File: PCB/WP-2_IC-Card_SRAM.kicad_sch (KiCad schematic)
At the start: 20 parts, among them J1 SMS-138-01-G-S, SW1 CUS-14TB, U1 AS6C4008

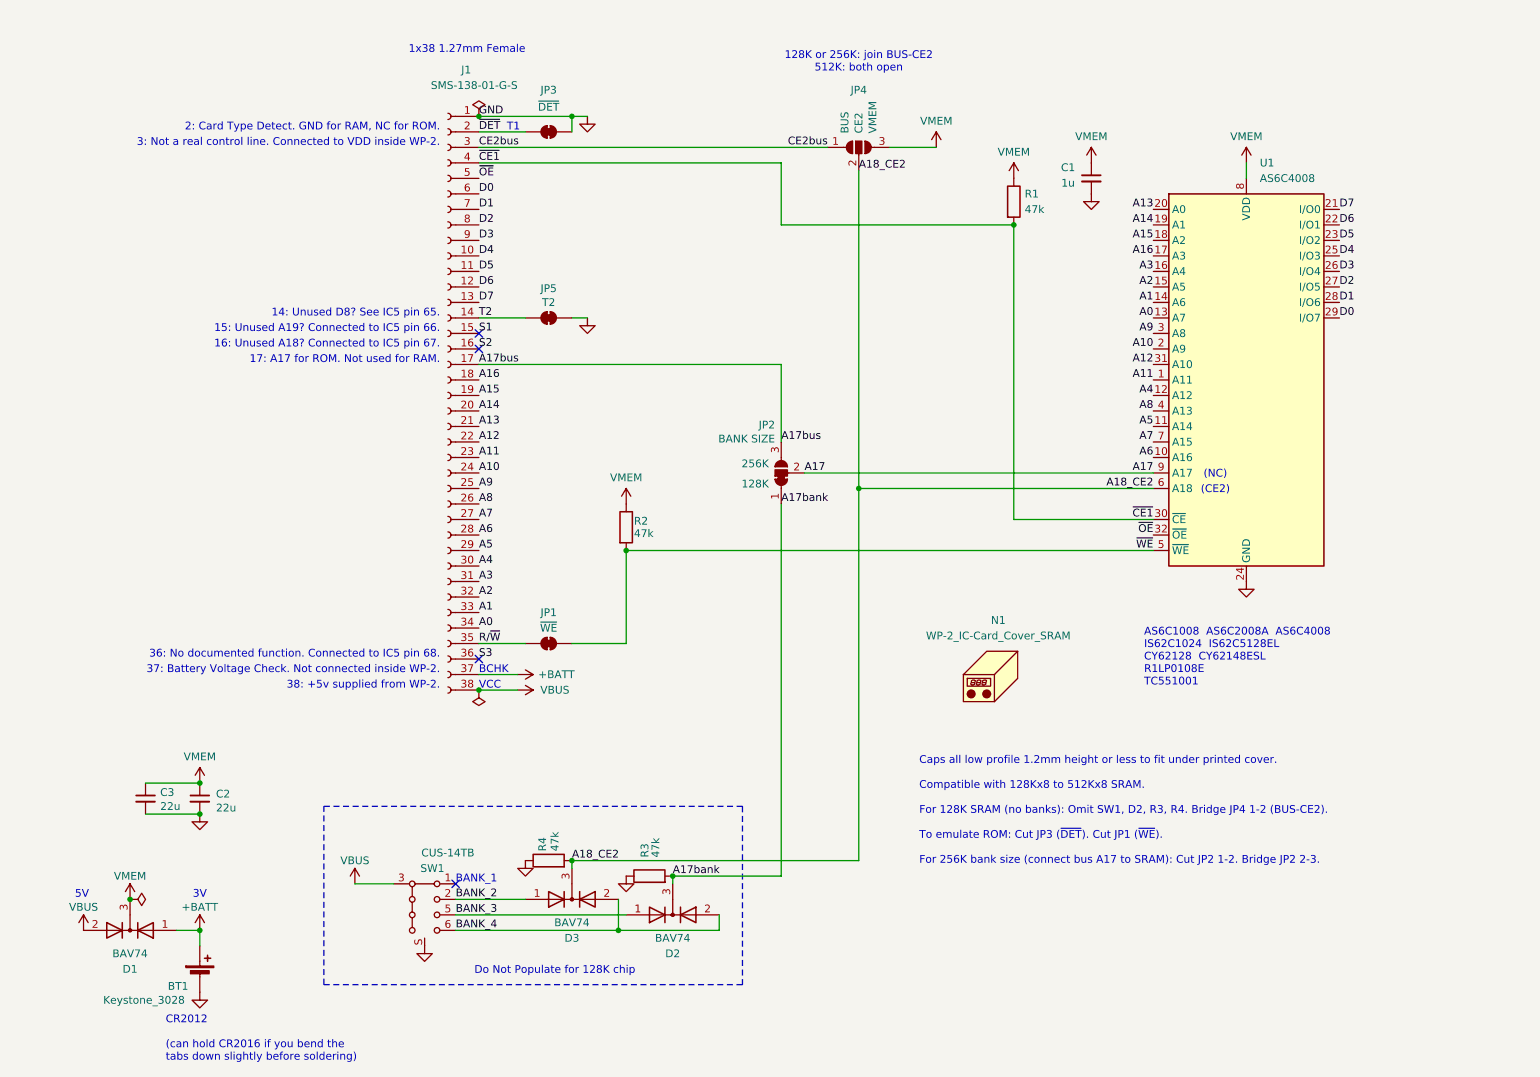
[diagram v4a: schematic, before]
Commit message: sram: resistors 100k, silkscreen, pics
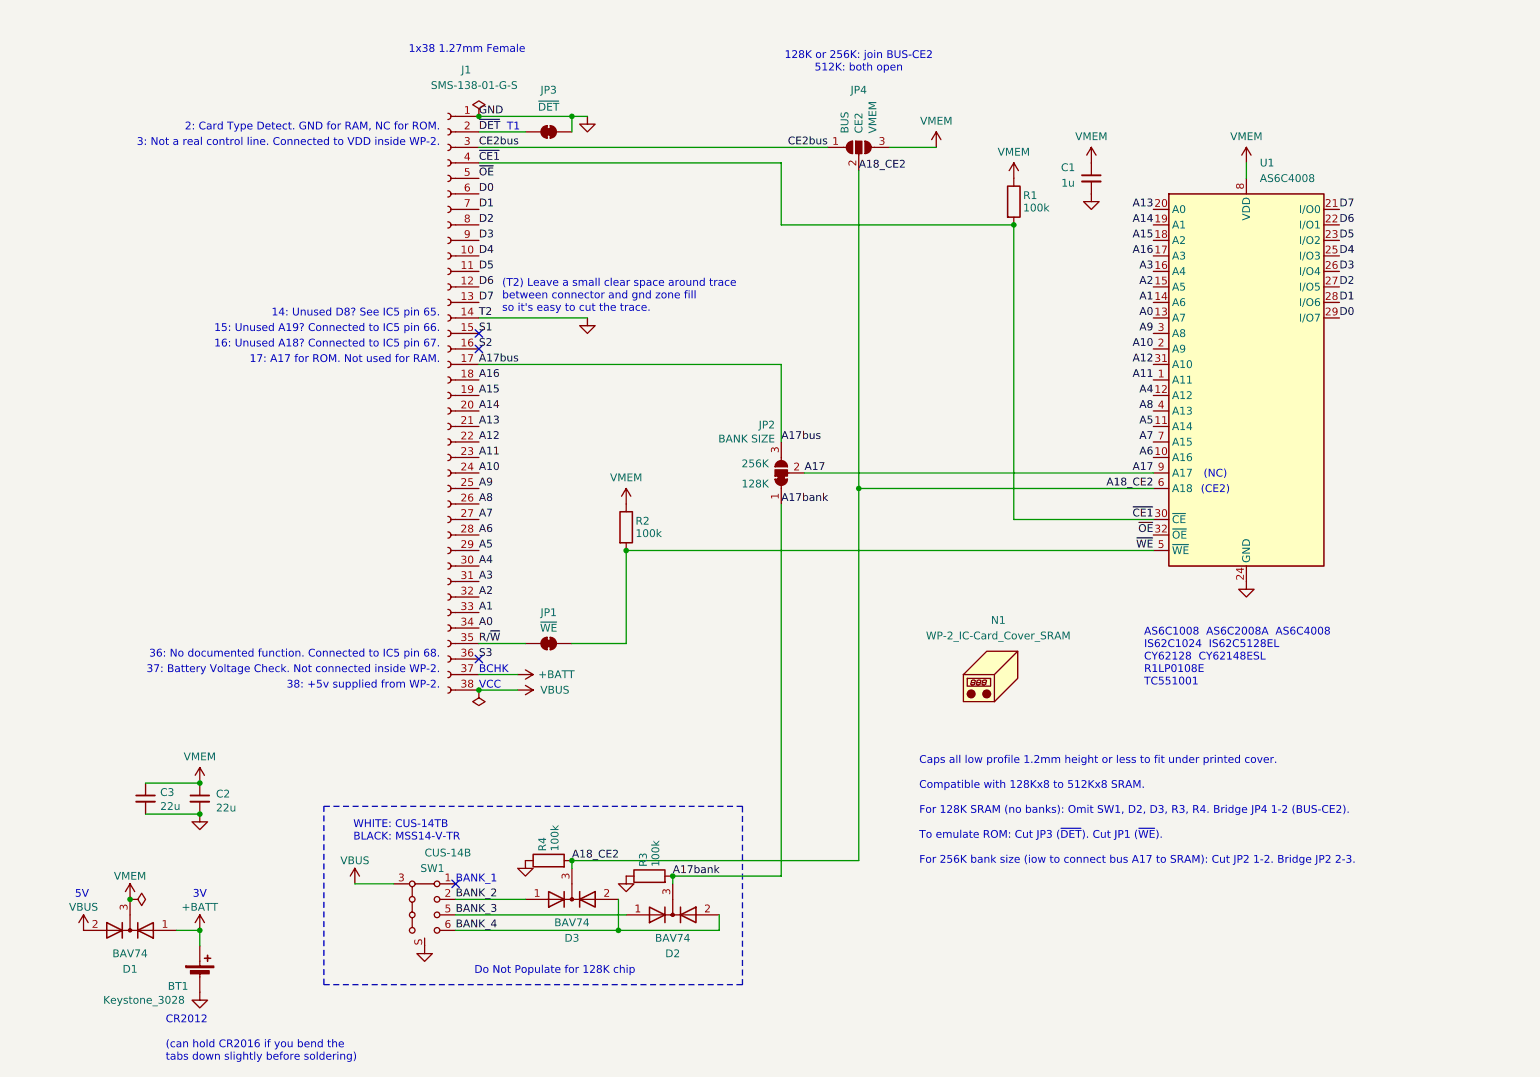
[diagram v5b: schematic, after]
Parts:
- removed JP5: T2, 000_LOCAL:SolderJumper-2_Bridged, symbol 000_LOCAL:SolderJumper_2_Bridged
- R1, R2, R3, R4: value 47k -> 100k; MPN RMCF0805FT47K0 -> RC0805FR-07100KL
- SW1: value CUS-14TB -> CUS-14B
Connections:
- net T2 is gone; now on net GND: J1.14 (Pin_14)
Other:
- note added: "(T2) Leave a small clear space around trace between connector and gnd zone fill so it's easy to cut the trace."
- note added: "Caps all low profile 1.2mm height or less to fit under printed cover. Compatible with 128Kx8 to 512Kx8 SRAM. For 128K SRAM (no banks): Omit SW1, D2, D3, R3, R4. Bridge JP4 1-2 (BUS-CE2). To emulate ROM: Cut JP3 (~{DET}). Cut JP1 (~{WE}). For 256K bank size (iow to connect bus A17 to SRAM): Cut JP2 1-2. Bridge JP2 2-3."
- note added: "WHITE: CUS-14TB BLACK: MSS14-V-TR"
- note removed: "Caps all low profile 1.2mm height or less to fit under printed cover. Compatible with 128Kx8 to 512Kx8 SRAM. For 128K SRAM (no banks): Omit SW1, D2, R3, R4. Bridge JP4 1-2 (BUS-CE2). To emulate ROM: Cut JP3 (~{DET}). Cut JP1 (~{WE}). For 256K bank size (connect bus A17 to SRAM): Cut JP2 1-2. Bridge JP2 2-3."

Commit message: silkscreens, board outlines, switch slider, covers fitment, copper to edge
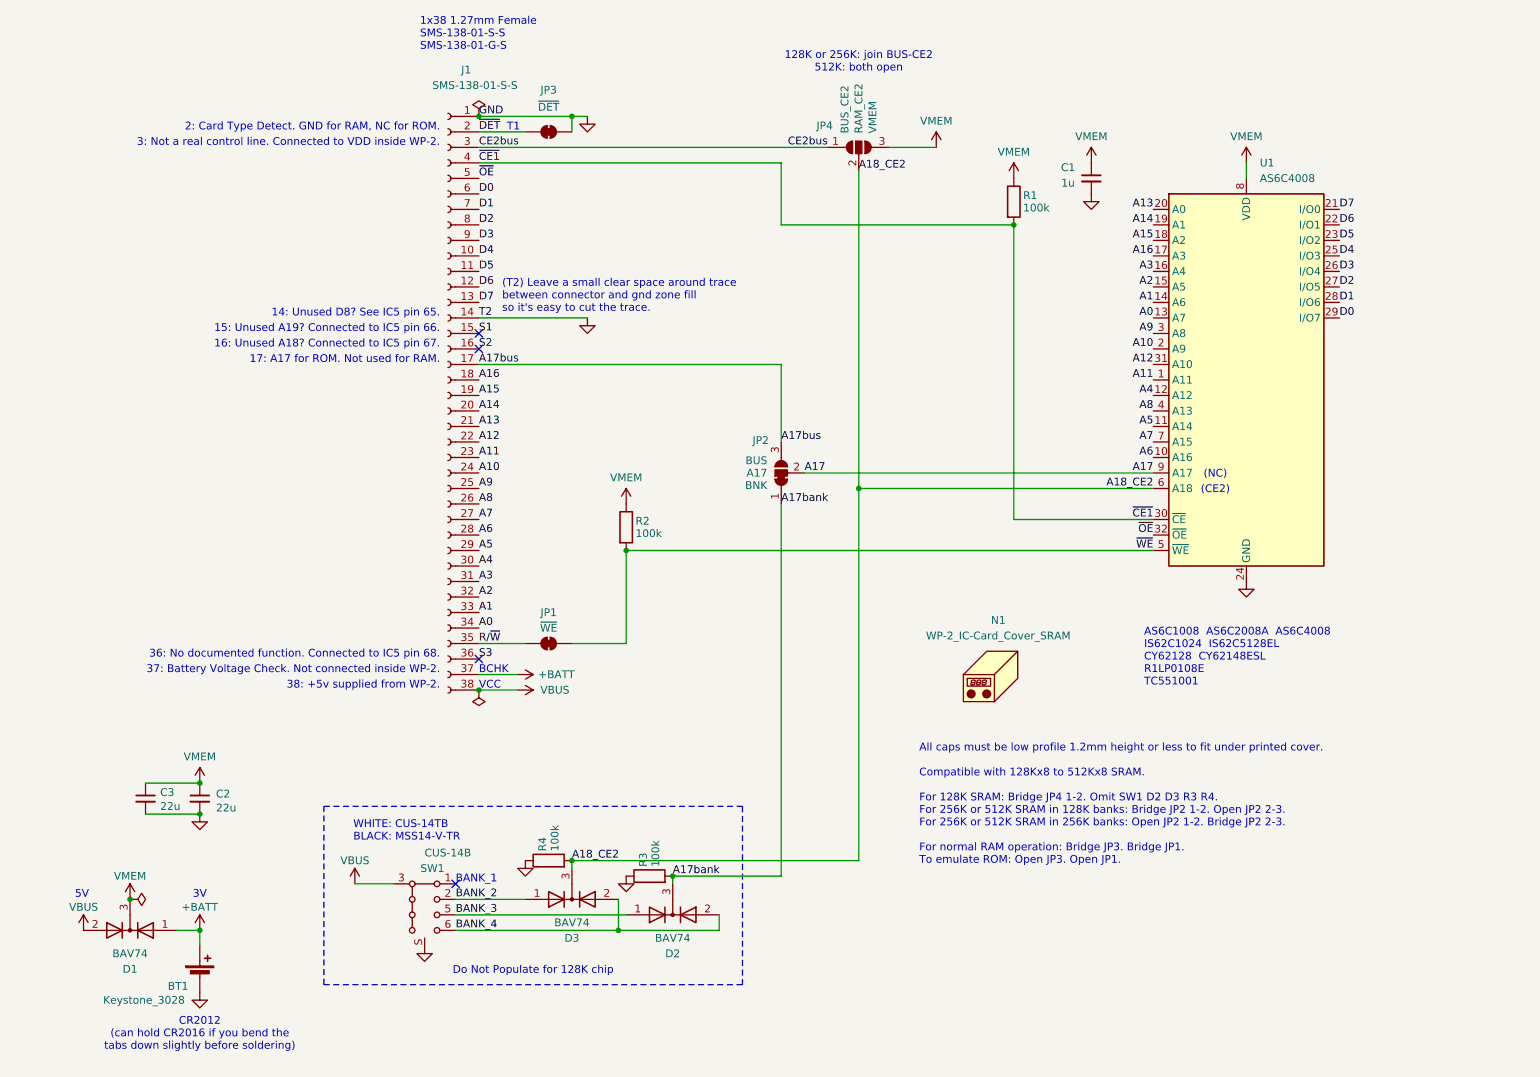
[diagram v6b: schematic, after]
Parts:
- J1: value SMS-138-01-G-S -> SMS-138-01-S-S; footprint 000_LOCAL:SMS-138-01-x-x_pcb_edge -> 000_LOCAL:SMS-138-01-x-S_pcb_edge
- JP2: value BANK SIZE -> A17; Label_1-2 128K -> BNK; Label_2-3 256K -> BUS
- JP4: value CE2 -> RAM_CE2; Label_1-2 BUS -> BUS_CE2
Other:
- note added: "1x38 1.27mm Female SMS-138-01-S-S SMS-138-01-G-S"
- note added: "All caps must be low profile 1.2mm height or less to fit under printed cover. Compatible with 128Kx8 to 512Kx8 SRAM. For 128K SRAM: Bridge JP4 1-2. Omit SW1 D2 D3 R3 R4. For 256K or 512K SRAM in 128K banks: Bridge JP2 1-2. Open JP2 2-3. For 256K or 512K SRAM in 256K banks: Open JP2 1-2. Bridge JP2 2-3. For normal RAM operation: Bridge JP3. Bridge JP1. To emulate ROM: Open JP3. Open JP1."
- note removed: "1x38 1.27mm Female"
- note removed: "Caps all low profile 1.2mm height or less to fit under printed cover. Compatible with 128Kx8 to 512Kx8 SRAM. For 128K SRAM (no banks): Omit SW1, D2, D3, R3, R4. Bridge JP4 1-2 (BUS-CE2). To emulate ROM: Cut JP3 (~{DET}). Cut JP1 (~{WE}). For 256K bank size (iow to connect bus A17 to SRAM): Cut JP2 1-2. Bridge JP2 2-3."
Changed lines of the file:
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@@
 		)
 	)
-	(text "1x38 1.27mm Female"
+	(text "1x38 1.27mm Female\nSMS-138-01-S-S\nSMS-138-01-G-S"
 		(exclude_from_sim no)
-		(at 97.79 35.56 0)
+		(at 80.518 35.052 0)
 		(effects
 			(font
 				(size 1.27 1.27)
 			)
-			(justify right bottom)
+			(justify left bottom)
 		)
 	)
@@
 		)
 	)
-	(text "CR2012\n\n(can hold CR2016 if you bend the\ntabs down slightly before soldering)"
+	(text "CR2012\n(can hold CR2016 if you bend the\ntabs down slightly before soldering)"
 		(exclude_from_sim no)
-		(at 38.862 193.04 0)
+		(at 44.45 193.294 0)
 		(effects
 			(font
 				(size 1.27 1.27)
 			)
-			(justify left top)
+			(justify top)
 		)
 	)
@@
 		)
 	)
-	(text "Caps all low profile 1.2mm height or less to fit under printed cover.\n\nCompatible with 128Kx8 to 512Kx8 SRAM.\n\nFor 128K SRAM (no banks): Omit SW1, D2, D3, R3, R4. Bridge JP4 1-2 (BUS-CE2).\n\nTo emulate ROM: Cut JP3 (~{DET}). Cut JP1 (~{WE}).\n\nFor 256K bank size (iow to connect bus A17 to SRAM): Cut JP2 1-2. Bridge JP2 2-3."
+	(text "All caps must be low profile 1.2mm height or less to fit under printed cover.\n\nCompatible with 128Kx8 to 512Kx8 SRAM.\n\nFor 128K SRAM: Bridge JP4 1-2. Omit SW1 D2 D3 R3 R4.\nFor 256K or 512K SRAM in 128K banks: Bridge JP2 1-2. Open JP2 2-3.\nFor 256K or 512K SRAM in 256K banks: Open JP2 1-2. Bridge JP2 2-3.\n\nFor normal RAM operation: Bridge JP3. Bridge JP1.\nTo emulate ROM: Open JP3. Open JP1.\n"
 		(exclude_from_sim no)
 		(at 162.306 168.402 0)
@@
 	(text "Do Not Populate for 128K chip"
 		(exclude_from_sim no)
-		(at 102.616 186.436 0)
+		(at 99.06 186.436 0)
 		(effects
 			(font
@@
 			)
 		)
-		(property "Value" "SMS-138-01-G-S"
+		(property "Value" "SMS-138-01-S-S"
 			(at 96.52 40.64 0)
 			(effects
@@
 			)
 		)
-		(property "Footprint" "000_LOCAL:SMS-138-01-x-x_pcb_edge"
+		(property "Footprint" "000_LOCAL:SMS-138-01-x-S_pcb_edge"
 			(at 85.09 91.44 0)
 			(effects
@@
 		(dnp no)
 		(property "Reference" "JP2"
-			(at 138.684 96.266 90)
+			(at 137.668 98.806 90)
 			(effects
 				(font
@@
 			)
 		)
-		(property "Value" "BANK SIZE"
-			(at 138.684 98.552 90)
+		(property "Value" "A17"
+			(at 137.414 104.14 90)
 			(effects
 				(font
@@
 			)
 		)
-		(property "Label_1-2" "128K"
-			(at 137.668 105.918 90)
+		(property "Label_1-2" "BNK"
+			(at 137.414 106.172 90)
 			(effects
 				(font
@@
 			)
 		)
-		(property "Label_2-3" "256K"
-			(at 137.668 102.616 90)
+		(property "Label_2-3" "BUS"
+			(at 137.414 102.108 90)
 			(effects
 				(font
@@
 		(dnp no)
 		(property "Reference" "JP4"
-			(at 152.4 41.402 0)
+			(at 146.812 47.244 0)
 			(effects
 				(font
@@
 			)
 		)
-		(property "Value" "CE2"
+		(property "Value" "RAM_CE2"
 			(at 152.4 48.514 90)
 			(effects
@@
 			)
 		)
-		(property "Label_1-2" "BUS"
+		(property "Label_1-2" "BUS_CE2"
 			(at 150.114 48.514 90)
 			(effects

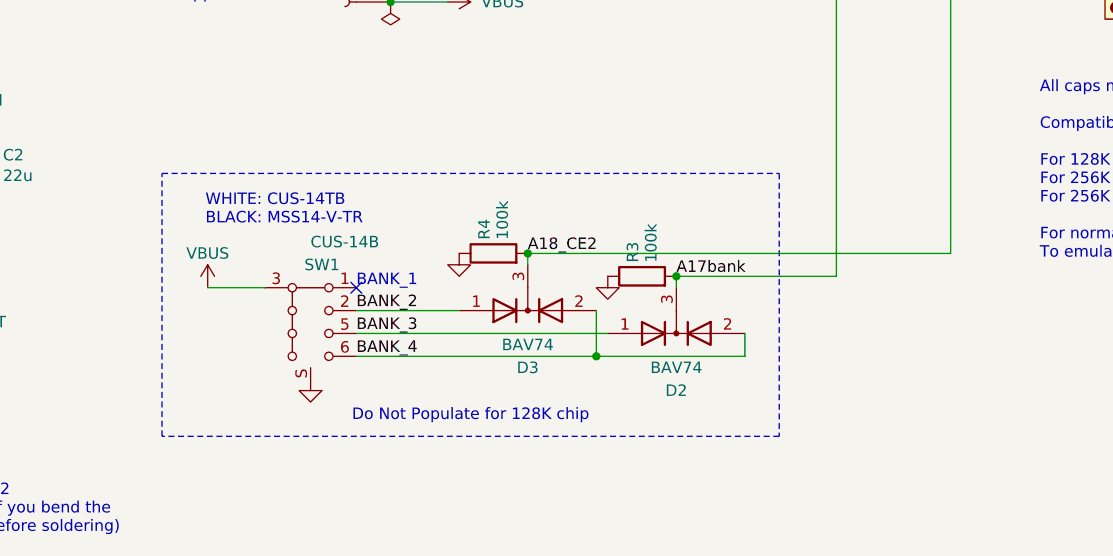
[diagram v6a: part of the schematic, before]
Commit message: MRAM: diodes, level shifters, ldo, docs
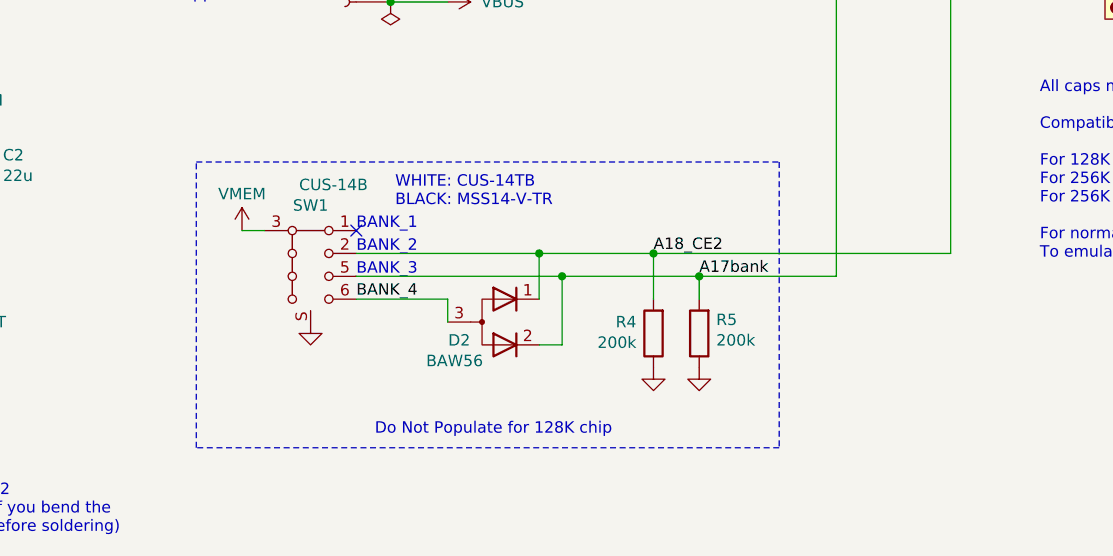
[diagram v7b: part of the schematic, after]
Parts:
- removed D2, D3: BAV74, 000_LOCAL:SOT-23, symbol 000_LOCAL:BAV170
- removed R3: 100k, 000_LOCAL:R_0805, symbol 000_LOCAL:R
- added D2: BAW56, 000_LOCAL:SOT-23, symbol 000_LOCAL:D_Dual_CommonAnode_KKA_Parallel
- added R5: 200k, 000_LOCAL:R_0805, symbol 000_LOCAL:R
- R4: value 100k -> 200k; MPN RC0805FR-07100KL -> RMCF0805FT200K
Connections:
- net BANK_2 is gone; now on net A18_CE2: SW1.2
- net BANK_3 is gone; now on net A17bank: SW1.5
- net A17bank: now also D2.2 (K), R5.2
- net A18_CE2: now also D2.1 (K)
- net BANK_4: now also D2.3 (A)
- net GND: now also R5.1
- net VBUS: no longer SW1.3 (C), SW1.4 (C)
- net VMEM: now also SW1.3 (C), SW1.4 (C)
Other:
- note added: "BANK_2"
- note added: "BANK_3"

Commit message: sram diodes
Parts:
- removed D2: BAW56, 000_LOCAL:SOT-23, symbol 000_LOCAL:D_Dual_CommonAnode_KKA_Parallel
- removed R5: 200k, 000_LOCAL:R_0805, symbol 000_LOCAL:R
- added D2, D3: BAV74, 000_LOCAL:SOT-23, symbol 000_LOCAL:BAV70
- added R3: 100k, 000_LOCAL:R_0805, symbol 000_LOCAL:R
- R4: value 200k -> 100k; MPN RMCF0805FT200K -> RC0805FR-07100KL
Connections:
- net A17bank: now also SW1.2, D2.3 (K), R3.2; no longer SW1.5
- net A18_CE2: now also SW1.5, D3.3 (K); no longer SW1.2
- net BANK_4: now also D2.2 (A), D3.1 (A)
- net GND: now also R3.1
- net R/~{W}: now also JP1.2 (B); no longer JP1.1 (A)
- net VBUS: now also SW1.3 (C), SW1.4 (C)
- net VMEM: no longer SW1.3 (C), SW1.4 (C)
- net ~{WE}: now also JP1.1 (A); no longer JP1.2 (B)
- no-connect marks 4 -> 6
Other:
- moved on the sheet: JP1
